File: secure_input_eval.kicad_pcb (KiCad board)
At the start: 6 copper layers, 99.8 x 99.9 mm, 79 parts, among them CON1_STLINK1 ST-LINK, J10 masa pomiarowa, J11 Conn 5 USB 1 A, J12 Conn 5 USB 1 B, J13 Conn_19 USBC FULL 1B, J14 USB_C_Receptacle FULL 2, J15 USB3_A_Stacked, J16 Conn 10 USB3 A1 A, J17 USB_C_Receptacle FULL 1, J18_CPU_CON1 Conn_CPU, J19 masa pomiarowa, J20 Conn_ 19USBC FULL 1A, J21 Conn 19 USBC FULL 2A, J22 Conn 19USBC FULL 2B, J23 masa pomiarowa, J24 masa pomiarowa, J25 masa pomiarowa, J26 masa pomiarowa, J27_USART3 USART, J28_PIN14_PA7 TOUCH_SINGLE, J29_D+_PIN23_PA12 D+_PP, J2_SD_SPI1 MEM2085-00-115-00-A_REV0.2, J30_D-_PIN22_PA11 D-_PP, J31_CS_PP_PIN7_PA0 CS_PP_PIN7_PA0, J32_MOSI_PIN9_PA2 MOSI_PP, J33_MISO_PP_PIN13_PA6 MISO_PP_PIN13_PA6, J34_SCK_PP_PIN8_PA1 SCK_PP_PIN8_PA1, J35_SCL_PP_PIN19_PA9 SCL_PP_PIN19_PA9, J36_SDA_PP_PIN1_PB9 SDA_PP_PIN1_PB9, J37 Conn 10 USB3 A1B, J3_SWO_NC1 SWO NC, J4 USB3_A_Stacked, J5 Conn 10 USB 3 A 2 A, J6 Conn 10 USB 3 A 2 B, J7 masa pomiarowa, J8 USB_A 1, J9 masa pomiarowa, SW1_PIN11_PA4 B3U-3000P, SW2_PIN32_PB8 B3U-3000P, SW3_PIN31_PB7 B3U-3000P, SW4_PIN26_PA15 B3U-3000P, SW5_TCH__PIN12_PA5 sensor dotykowy_PIN12_PA5, SW6_PIN25_PA14 BOOT0, U1 STM32G0B1KETx, U2 LD1117-3.3

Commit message: Update  conector usb.
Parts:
- added J1: USB_C_Receptacle_USB2.0_16P, Connector_USB:USB_C_Receptacle_G-Switch_GT-USB-7010ASV, F.Cu at (143.0, 59.5)
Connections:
- net /PIN21_PA10 renamed /FINGER_SENSOR_SDA
- J18_CPU_CON1 pad 10: /PIN10_PA3 -> /SW7_touch_single
- U1 pad 10: /PIN10_PA3 -> /SW7_touch_single
- U1 pad 14: /SW7_touch_single -> /FINGER_SENSOR_SCL

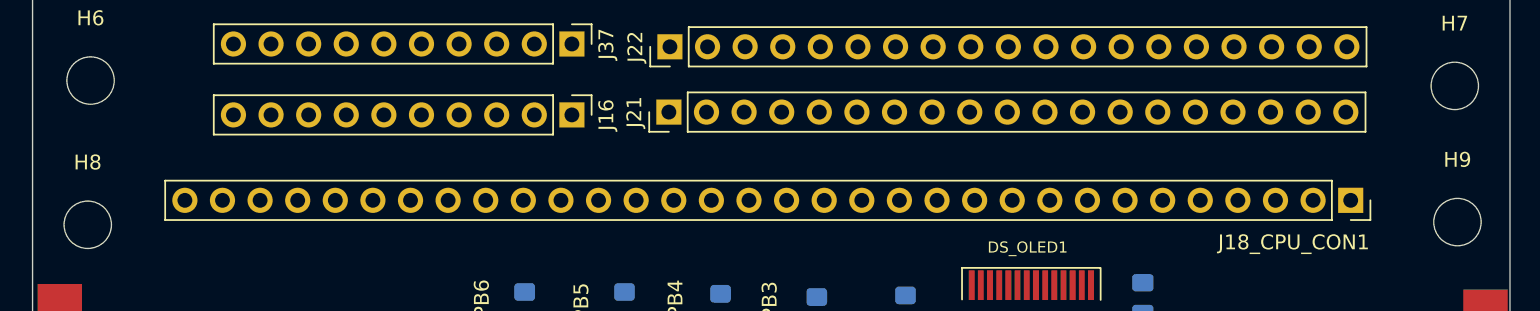
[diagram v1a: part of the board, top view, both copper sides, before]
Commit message: Cutting two bards drill-holes.
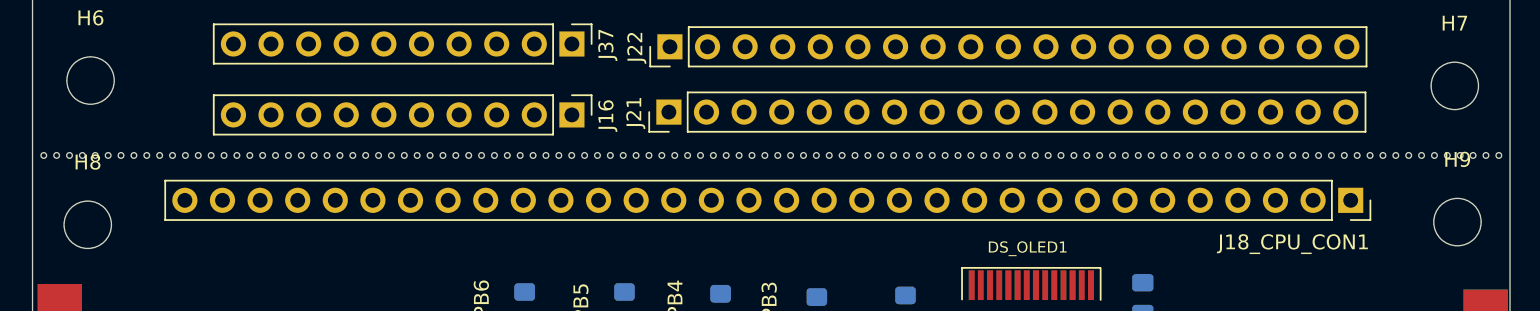
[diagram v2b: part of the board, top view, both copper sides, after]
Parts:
- added REF**: MountingHole_1mm, secure_input_pen:MountingHole_1mm, F.Cu at (131.6, 85.9)
- added REF**: MountingHole_1mm, secure_input_pen:MountingHole_1mm, F.Cu at (63.8, 85.9)
- added REF**: MountingHole_1mm, secure_input_pen:MountingHole_1mm, F.Cu at (89.0, 85.9)
- added REF**: MountingHole_1mm, secure_input_pen:MountingHole_1mm, F.Cu at (130.7, 85.9)
- added REF**: MountingHole_1mm, secure_input_pen:MountingHole_1mm, F.Cu at (121.2, 85.9)
- added REF**: MountingHole_1mm, secure_input_pen:MountingHole_1mm, F.Cu at (49.9, 85.9)
- added REF**: MountingHole_1mm, secure_input_pen:MountingHole_1mm, F.Cu at (68.1, 85.9)
- added REF**: MountingHole_1mm, secure_input_pen:MountingHole_1mm, F.Cu at (90.7, 85.9)
- added REF**: MountingHole_1mm, secure_input_pen:MountingHole_1mm, F.Cu at (132.5, 85.9)
- added REF**: MountingHole_1mm, secure_input_pen:MountingHole_1mm, F.Cu at (124.7, 85.9)
- added REF**: MountingHole_1mm, secure_input_pen:MountingHole_1mm, F.Cu at (56.0, 85.9)
- added REF**: MountingHole_1mm, secure_input_pen:MountingHole_1mm, F.Cu at (113.4, 85.9)
- added REF**: MountingHole_1mm, secure_input_pen:MountingHole_1mm, F.Cu at (126.4, 85.9)
- added REF**: MountingHole_1mm, secure_input_pen:MountingHole_1mm, F.Cu at (110.7, 85.9)
- added REF**: MountingHole_1mm, secure_input_pen:MountingHole_1mm, F.Cu at (84.7, 85.9)
- added REF**: MountingHole_1mm, secure_input_pen:MountingHole_1mm, F.Cu at (65.5, 85.9)
- added REF**: MountingHole_1mm, secure_input_pen:MountingHole_1mm, F.Cu at (123.8, 85.9)
- added REF**: MountingHole_1mm, secure_input_pen:MountingHole_1mm, F.Cu at (60.3, 85.9)
- added REF**: MountingHole_1mm, secure_input_pen:MountingHole_1mm, F.Cu at (102.0, 85.9)
- added REF**: MountingHole_1mm, secure_input_pen:MountingHole_1mm, F.Cu at (99.4, 85.9)
- added REF**: MountingHole_1mm, secure_input_pen:MountingHole_1mm, F.Cu at (129.9, 85.9)
- added REF**: MountingHole_1mm, secure_input_pen:MountingHole_1mm, F.Cu at (143.8, 85.9)
- added REF**: MountingHole_1mm, secure_input_pen:MountingHole_1mm, F.Cu at (71.6, 85.9)
- added REF**: MountingHole_1mm, secure_input_pen:MountingHole_1mm, F.Cu at (87.3, 85.9)
- added REF**: MountingHole_1mm, secure_input_pen:MountingHole_1mm, F.Cu at (107.3, 85.9)
- added REF**: MountingHole_1mm, secure_input_pen:MountingHole_1mm, F.Cu at (62.9, 85.9)
- added REF**: MountingHole_1mm, secure_input_pen:MountingHole_1mm, F.Cu at (96.0, 85.9)
- added REF**: MountingHole_1mm, secure_input_pen:MountingHole_1mm, F.Cu at (96.8, 85.9)
- added REF**: MountingHole_1mm, secure_input_pen:MountingHole_1mm, F.Cu at (144.7, 85.9)
- added REF**: MountingHole_1mm, secure_input_pen:MountingHole_1mm, F.Cu at (108.1, 85.9)
- added REF**: MountingHole_1mm, secure_input_pen:MountingHole_1mm, F.Cu at (82.9, 85.9)
- added REF**: MountingHole_1mm, secure_input_pen:MountingHole_1mm, F.Cu at (137.7, 85.9)
- added REF**: MountingHole_1mm, secure_input_pen:MountingHole_1mm, F.Cu at (101.2, 85.9)
- added REF**: MountingHole_1mm, secure_input_pen:MountingHole_1mm, F.Cu at (53.3, 85.9)
- added REF**: MountingHole_1mm, secure_input_pen:MountingHole_1mm, F.Cu at (69.9, 85.9)
- added REF**: MountingHole_1mm, secure_input_pen:MountingHole_1mm, F.Cu at (57.7, 85.9)
- added REF**: MountingHole_1mm, secure_input_pen:MountingHole_1mm, F.Cu at (125.5, 85.9)
- added REF**: MountingHole_1mm, secure_input_pen:MountingHole_1mm, F.Cu at (118.6, 85.9)
- added REF**: MountingHole_1mm, secure_input_pen:MountingHole_1mm, F.Cu at (145.5, 85.9)
- added REF**: MountingHole_1mm, secure_input_pen:MountingHole_1mm, F.Cu at (102.9, 85.9)
- added REF**: MountingHole_1mm, secure_input_pen:MountingHole_1mm, F.Cu at (77.7, 85.9)
- added REF**: MountingHole_1mm, secure_input_pen:MountingHole_1mm, F.Cu at (54.2, 85.9)
- added REF**: MountingHole_1mm, secure_input_pen:MountingHole_1mm, F.Cu at (73.4, 85.9)
- added REF**: MountingHole_1mm, secure_input_pen:MountingHole_1mm, F.Cu at (78.6, 85.9)
- added REF**: MountingHole_1mm, secure_input_pen:MountingHole_1mm, F.Cu at (141.2, 85.9)
- added REF**: MountingHole_1mm, secure_input_pen:MountingHole_1mm, F.Cu at (79.4, 85.9)
- added REF**: MountingHole_1mm, secure_input_pen:MountingHole_1mm, F.Cu at (70.7, 85.9)
- added REF**: MountingHole_1mm, secure_input_pen:MountingHole_1mm, F.Cu at (49.0, 85.9)
- added REF**: MountingHole_1mm, secure_input_pen:MountingHole_1mm, F.Cu at (129.0, 85.9)
- added REF**: MountingHole_1mm, secure_input_pen:MountingHole_1mm, F.Cu at (98.6, 85.9)
- added REF**: MountingHole_1mm, secure_input_pen:MountingHole_1mm, F.Cu at (69.0, 85.9)
- added REF**: MountingHole_1mm, secure_input_pen:MountingHole_1mm, F.Cu at (133.4, 85.9)
- added REF**: MountingHole_1mm, secure_input_pen:MountingHole_1mm, F.Cu at (82.0, 85.9)
- added REF**: MountingHole_1mm, secure_input_pen:MountingHole_1mm, F.Cu at (112.5, 85.9)
- added REF**: MountingHole_1mm, secure_input_pen:MountingHole_1mm, F.Cu at (61.2, 85.9)
- added REF**: MountingHole_1mm, secure_input_pen:MountingHole_1mm, F.Cu at (52.5, 85.9)
- added REF**: MountingHole_1mm, secure_input_pen:MountingHole_1mm, F.Cu at (72.5, 85.9)
- added REF**: MountingHole_1mm, secure_input_pen:MountingHole_1mm, F.Cu at (100.3, 85.9)
- added REF**: MountingHole_1mm, secure_input_pen:MountingHole_1mm, F.Cu at (94.2, 85.9)
- added REF**: MountingHole_1mm, secure_input_pen:MountingHole_1mm, F.Cu at (86.4, 85.9)
- added REF**: MountingHole_1mm, secure_input_pen:MountingHole_1mm, F.Cu at (114.2, 85.9)
- added REF**: MountingHole_1mm, secure_input_pen:MountingHole_1mm, F.Cu at (76.0, 85.9)
- added REF**: MountingHole_1mm, secure_input_pen:MountingHole_1mm, F.Cu at (103.8, 85.9)
- added REF**: MountingHole_1mm, secure_input_pen:MountingHole_1mm, F.Cu at (93.4, 85.9)
- added REF**: MountingHole_1mm, secure_input_pen:MountingHole_1mm, F.Cu at (128.1, 85.9)
- added REF**: MountingHole_1mm, secure_input_pen:MountingHole_1mm, F.Cu at (135.1, 85.9)
- added REF**: MountingHole_1mm, secure_input_pen:MountingHole_1mm, F.Cu at (106.4, 85.9)
- added REF**: MountingHole_1mm, secure_input_pen:MountingHole_1mm, F.Cu at (88.1, 85.9)
- added REF**: MountingHole_1mm, secure_input_pen:MountingHole_1mm, F.Cu at (136.8, 85.9)
- added REF**: MountingHole_1mm, secure_input_pen:MountingHole_1mm, F.Cu at (111.6, 85.9)
- added REF**: MountingHole_1mm, secure_input_pen:MountingHole_1mm, F.Cu at (117.7, 85.9)
- added REF**: MountingHole_1mm, secure_input_pen:MountingHole_1mm, F.Cu at (80.3, 85.9)
- added REF**: MountingHole_1mm, secure_input_pen:MountingHole_1mm, F.Cu at (104.7, 85.9)
- added REF**: MountingHole_1mm, secure_input_pen:MountingHole_1mm, F.Cu at (75.1, 85.9)
- added REF**: MountingHole_1mm, secure_input_pen:MountingHole_1mm, F.Cu at (122.1, 85.9)
- added REF**: MountingHole_1mm, secure_input_pen:MountingHole_1mm, F.Cu at (95.1, 85.9)
- added REF**: MountingHole_1mm, secure_input_pen:MountingHole_1mm, F.Cu at (74.2, 85.9)
- added REF**: MountingHole_1mm, secure_input_pen:MountingHole_1mm, F.Cu at (142.1, 85.9)
- added REF**: MountingHole_1mm, secure_input_pen:MountingHole_1mm, F.Cu at (97.7, 85.9)
- added REF**: MountingHole_1mm, secure_input_pen:MountingHole_1mm, F.Cu at (56.8, 85.9)
- added REF**: MountingHole_1mm, secure_input_pen:MountingHole_1mm, F.Cu at (122.9, 85.9)
- added REF**: MountingHole_1mm, secure_input_pen:MountingHole_1mm, F.Cu at (58.6, 85.9)
- added REF**: MountingHole_1mm, secure_input_pen:MountingHole_1mm, F.Cu at (92.5, 85.9)
- added REF**: MountingHole_1mm, secure_input_pen:MountingHole_1mm, F.Cu at (120.3, 85.9)
- added REF**: MountingHole_1mm, secure_input_pen:MountingHole_1mm, F.Cu at (85.5, 85.9)
- added REF**: MountingHole_1mm, secure_input_pen:MountingHole_1mm, F.Cu at (76.8, 85.9)
- added REF**: MountingHole_1mm, secure_input_pen:MountingHole_1mm, F.Cu at (66.4, 85.9)
- added REF**: MountingHole_1mm, secure_input_pen:MountingHole_1mm, F.Cu at (50.7, 85.9)
- added REF**: MountingHole_1mm, secure_input_pen:MountingHole_1mm, F.Cu at (119.4, 85.9)
- added REF**: MountingHole_1mm, secure_input_pen:MountingHole_1mm, F.Cu at (115.1, 85.9)
- added REF**: MountingHole_1mm, secure_input_pen:MountingHole_1mm, F.Cu at (109.0, 85.9)
- added REF**: MountingHole_1mm, secure_input_pen:MountingHole_1mm, F.Cu at (62.0, 85.9)
- added REF**: MountingHole_1mm, secure_input_pen:MountingHole_1mm, F.Cu at (138.6, 85.9)
- added REF**: MountingHole_1mm, secure_input_pen:MountingHole_1mm, F.Cu at (109.9, 85.9)
- added REF**: MountingHole_1mm, secure_input_pen:MountingHole_1mm, F.Cu at (81.2, 85.9)
- added REF**: MountingHole_1mm, secure_input_pen:MountingHole_1mm, F.Cu at (51.6, 85.9)
- added REF**: MountingHole_1mm, secure_input_pen:MountingHole_1mm, F.Cu at (142.9, 85.9)
- added REF**: MountingHole_1mm, secure_input_pen:MountingHole_1mm, F.Cu at (91.6, 85.9)
- added REF**: MountingHole_1mm, secure_input_pen:MountingHole_1mm, F.Cu at (83.8, 85.9)
- added REF**: MountingHole_1mm, secure_input_pen:MountingHole_1mm, F.Cu at (48.1, 85.9)
- added REF**: MountingHole_1mm, secure_input_pen:MountingHole_1mm, F.Cu at (59.4, 85.9)
- added REF**: MountingHole_1mm, secure_input_pen:MountingHole_1mm, F.Cu at (64.7, 85.9)
- added REF**: MountingHole_1mm, secure_input_pen:MountingHole_1mm, F.Cu at (89.9, 85.9)
- added REF**: MountingHole_1mm, secure_input_pen:MountingHole_1mm, F.Cu at (55.1, 85.9)
- added REF**: MountingHole_1mm, secure_input_pen:MountingHole_1mm, F.Cu at (146.4, 85.9)
- added REF**: MountingHole_1mm, secure_input_pen:MountingHole_1mm, F.Cu at (116.8, 85.9)
- added REF**: MountingHole_1mm, secure_input_pen:MountingHole_1mm, F.Cu at (67.3, 85.9)
- added REF**: MountingHole_1mm, secure_input_pen:MountingHole_1mm, F.Cu at (105.5, 85.9)
- added REF**: MountingHole_1mm, secure_input_pen:MountingHole_1mm, F.Cu at (139.4, 85.9)
- added REF**: MountingHole_1mm, secure_input_pen:MountingHole_1mm, F.Cu at (140.3, 85.9)
- added REF**: MountingHole_1mm, secure_input_pen:MountingHole_1mm, F.Cu at (127.3, 85.9)
- added REF**: MountingHole_1mm, secure_input_pen:MountingHole_1mm, F.Cu at (136.0, 85.9)
- added REF**: MountingHole_1mm, secure_input_pen:MountingHole_1mm, F.Cu at (116.0, 85.9)
- added REF**: MountingHole_1mm, secure_input_pen:MountingHole_1mm, F.Cu at (134.2, 85.9)

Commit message: TITLES&SUBTITLES POSITIONS & NAMES.
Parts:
- moved DS_OLED1 15.1 mm to (118.1, 108.4)
- moved U1 11.9 mm to (80.3, 118.8)
- moved R5 7.98 mm to (79.6, 104.0)
- moved R6 7.98 mm to (86.3, 104.0)
- moved D1_LEDR_PIN30_PB6 7.98 mm to (80.0, 110.3)
- moved D2_LEDB_PIN29_PB5 7.98 mm to (86.4, 110.4)
- moved D3_LEDG_PIN28_PB4 7.98 mm to (92.9, 110.4)
- moved D4_LEDY_PIN27_PB3 7.98 mm to (99.3, 110.4)
- moved R7 7.98 mm to (92.8, 104.1)
- moved R8 7.98 mm to (99.3, 104.4)
- moved R3 7.98 mm to (105.5, 109.0)
- moved R4 7.98 mm to (105.3, 104.2)
- moved J27_USART3 7.54 mm to (66.6, 111.4)
- moved J3_SWO_NC1 6.47 mm to (66.5, 116.8)
- moved SD_J2_SD_SPI1 3.97 mm to (136.2, 112.8)
- renumbered J35_SCL_PP_PIN19_PA9 to OLED_J35_SCL_PP_PIN19_PA9, J36_SDA_PP_PIN1_PB9 to OLED_J36_SDA_PP_PIN1_PB9, J2_SD_SPI1 to SD_J2_SD_SPI1, J31_CS_PP_PIN7_PA0 to SD_J31_CS_PP_PIN7_PA0, J32_MOSI_PIN9_PA2 to SD_J32_MOSI_PIN9_PA2, J33_MISO_PP_PIN13_PA6 to SD_J33_MISO_PP_PIN13_PA6, J34_SCK_PP_PIN8_PA1 to SD_J34_SCK_PP_PIN8_PA1
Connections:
- J18_CPU_CON1 pad 14: /SW7_touch_single -> /SW5_TCH
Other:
- board text added: "10| D+_PIN23_PA12/10"
- board text added: "11| D-_PIN22_PA11/9"
- board text added: "12| FNGR_SNSR_SDA_PIN21_PA10"
- board text added: "13| NOT_CONNECTED_PIN20_PC6"
- board text added: "14| OLED_SCL_PIN19_PA9"
- board text added: "15| NOT_CONNECTED_PIN18_PA8"
- board text added: "16| USART3_TX_PIN_17_PB2"
- board text added: "17| NOT_CONNECTED_PIN16_PB1"
- board text added: "18| USART3_RX_PIN_15_PB0"
- board text added: "19| SW7_touch_single_PIN10_PA3"
- board text added: "1| SW2_PIN32_PB8"
- board text added: "20| SD_MISO_PIN13_PA6"
- board text added: "21| SW5_TCH_PIN12_PA5"
- board text added: "22| SW1_PIN11_PA4"
- board text added: "23| SW7_tch_singl_PIN10_PA3"
- board text added: "24| SD_MOSI_PIN9_PA2"
- board text added: "25| SD_SCK_PIN8_PA1"
- board text added: "26| SD_CS_PIN7_PA0"
- board text added: "27| RESET_PIN6_PF2"
- board text added: "28| masa_VSS_PIN5"
- board text added: "29| +3,3_VDD_PIN4"
- board text added: "2| SW3_PIN31_PB7"
- board text added: "30| NOT_CONNECTED_PIN3_PC15"
- board text added: "31| NOT_CONNECTED_PIN2_PC14"
- board text added: "32| OLED_SDA_PIN1_PB9"
- board text added: "3| D1_LEDR_PIN30_PB6"
- board text added: "4| D2_LEDB_PIN29_PB5"
- board text added: "5| D3_LEDG_PIN28_PB4"
- board text added: "6| D4_LEDY_PIN27_PB3"
- board text added: "7| SW4_PIN26_PA15"
- board text added: "8| SWCLK_PIN25_PA14"
- board text added: "9| SWDIO_PIN24_PA13"
- board text added: "BOOT"

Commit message: symbole i footprinty #1
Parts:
- added J2: USB3_A, foots6:USB3_A_Amphenol_GSB316441CEU, F.Cu at (33.1, 34.1)
- H5: footprint secure_input_pen:MountingHole_2mm -> foots6:MountingHole_2mm
- J8: footprint Connector_USB:USB_A_CONNFLY_DS1095-WNR0 -> Connector_USB:USB_A_Connfly_DS1095
- renumbered SD_J31_CS_PP_PIN7_PA0 to J31_CS_PP_PIN7_PA0, SD_J32_MOSI_PIN9_PA2 to J32_MOSI_PIN9_PA2, SD_J33_MISO_PP_PIN13_PA6 to J33_MISO_PP_PIN13_PA6, SD_J34_SCK_PP_PIN8_PA1 to J34_SCK_PP_PIN8_PA1, OLED_J35_SCL_PP_PIN19_PA9 to J35_SCL_PP_PIN19_PA9, OLED_J36_SDA_PP_PIN1_PB9 to J36_SDA_PP_PIN1_PB9, SD_J2_SD_SPI1 to J38_SD_SPI1
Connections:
- J38_SD_SPI1 pad CD: unconnected-(J2_SD_SPI1-PadCD) -> (no net)
- J38_SD_SPI1 pad P1: unconnected-(J2_SD_SPI1-DAT2-PadP1) -> (no net)
- J38_SD_SPI1 pad P8: unconnected-(J2_SD_SPI1-DAT1-PadP8) -> (no net)
